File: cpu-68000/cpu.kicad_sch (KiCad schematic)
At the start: 21 parts

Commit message: added memory, peripherals
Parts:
- removed C?: 100nF, symbol Device:C_Small
- removed X?: 10MHz, Oscillator:Oscillator_DIP-8, symbol Oscillator:CXO_DIP8
- added C?: 22µF, symbol Device:C_Polarized_Small
- added C?: 100nF, symbol Device:C_Small
- added C?: 1µF, symbol Device:C_Small
- added R?: 1k, symbol Device:R_Small
- added R? (x2): 10k, symbol Device:R_Small
- added U? (x2): 74HC05, symbol 74xx:74LS05
- added U?: TL7733B, symbol Power_Supervisor:TL7733B
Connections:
- net +5V: now also C?.1, R?.2, U?.7 (SENSE), U?.8 (VCC)
- net GND: now also C?.2, C?.2, C?.2, R?.1, U?.4 (GND)
- net ~{HALT}: now also U?.8
- net ~{RESET}: now also U?.6
- new net: C?.1, U?.1 (REF)
- new net: C?.1, R?.1
- new net: R?.2, U?.3 (CT)
- new net: R?.1, U?.5 (~{RESET})
- new net POR: R?.2, U?.5, U?.6 (RESET), U?.9
- new net ~{MRES}: U?.2 (~{RESIN})
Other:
- note added: "Power on Reset Circuit"

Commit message: Peripherals and general connection stuff
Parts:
- removed C?: 100nF, symbol Device:C_Small
- removed D?: LED_Dual_AKAK, symbol Device:LED_Dual_AKAK
- removed R? (x2): 1k, symbol Device:R_Small
- removed U? (x4): 74HC04, symbol 74xx:74HC04
- added RN? (x2): 10k, Resistor_THT:R_Array_SIP9, symbol Device:R_Network08
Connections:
- net AS: now also U?.15 (IO2)
- net D0: now also RN?.9 (R8)
- net D1: now also RN?.8 (R7)
- net D10: now also RN?.7 (R6)
- net D11: now also RN?.6 (R5)
- net D12: now also RN?.5 (R4)
- net D13: now also RN?.4 (R3)
- net D14: now also RN?.3 (R2)
- net D15: now also RN?.2 (R1)
- net D2: now also RN?.7 (R6)
- net D3: now also RN?.6 (R5)
- net D4: now also RN?.5 (R4)
- net D5: now also RN?.4 (R3)
- net D6: now also RN?.3 (R2)
- net D7: now also RN?.2 (R1)
- net D8: now also RN?.9 (R8)
- net D9: now also RN?.8 (R7)
- net GND: now also RN?.1 (common), RN?.1 (common)
- net ~{AS}: now also U?.14 (IO1)
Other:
- note added: "IRQ Level Encoder"
- note added: "IRQ, addr space decoder"

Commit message: More backplane stuff; added footprints for most
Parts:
- removed C?: 22µF, symbol Device:C_Polarized_Small
- added R301: 1k, Resistor_SMD:R_0805_2012Metric, symbol Device:R_Small
- added R302, R303: 10k, Resistor_SMD:R_0805_2012Metric, symbol Device:R_Small
- C301: renamed from C?; footprint (none) -> Capacitor_Tantalum_SMD:CP_EIA-3216-18_Kemet-A
- C302, C303, C304, C306, C307, C308, C309, C310: renamed from C?; footprint (none) -> Capacitor_SMD:C_0805_2012Metric
- R304, R305, R306: renamed from R?; footprint (none) -> Resistor_SMD:R_0805_2012Metric
- U104: renamed from U?; footprint (none) -> Package_SO:SOIC-14_3.9x8.7mm_P1.27mm
- U301: renamed from U?; footprint Package_LCC:PLCC-68 -> Package_LCC:PLCC-68_THT-Socket
- U303: renamed from U?; footprint (none) -> Package_SO:SOIC-8_3.9x4.9mm_P1.27mm
- U304: renamed from U?; footprint (none) -> Package_SO:TSSOP-16_4.4x5mm_P0.65mm; MPN (none) -> 74HC175PW,118
- gave numbers to parts that had none: 4
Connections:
- net +5V: now also R301.1, R302.1, R303.1
- net ~{BGACK}: now also R303.2
- net ~{BR}: now also R302.2
- net ~{DTACK}: now also R301.2

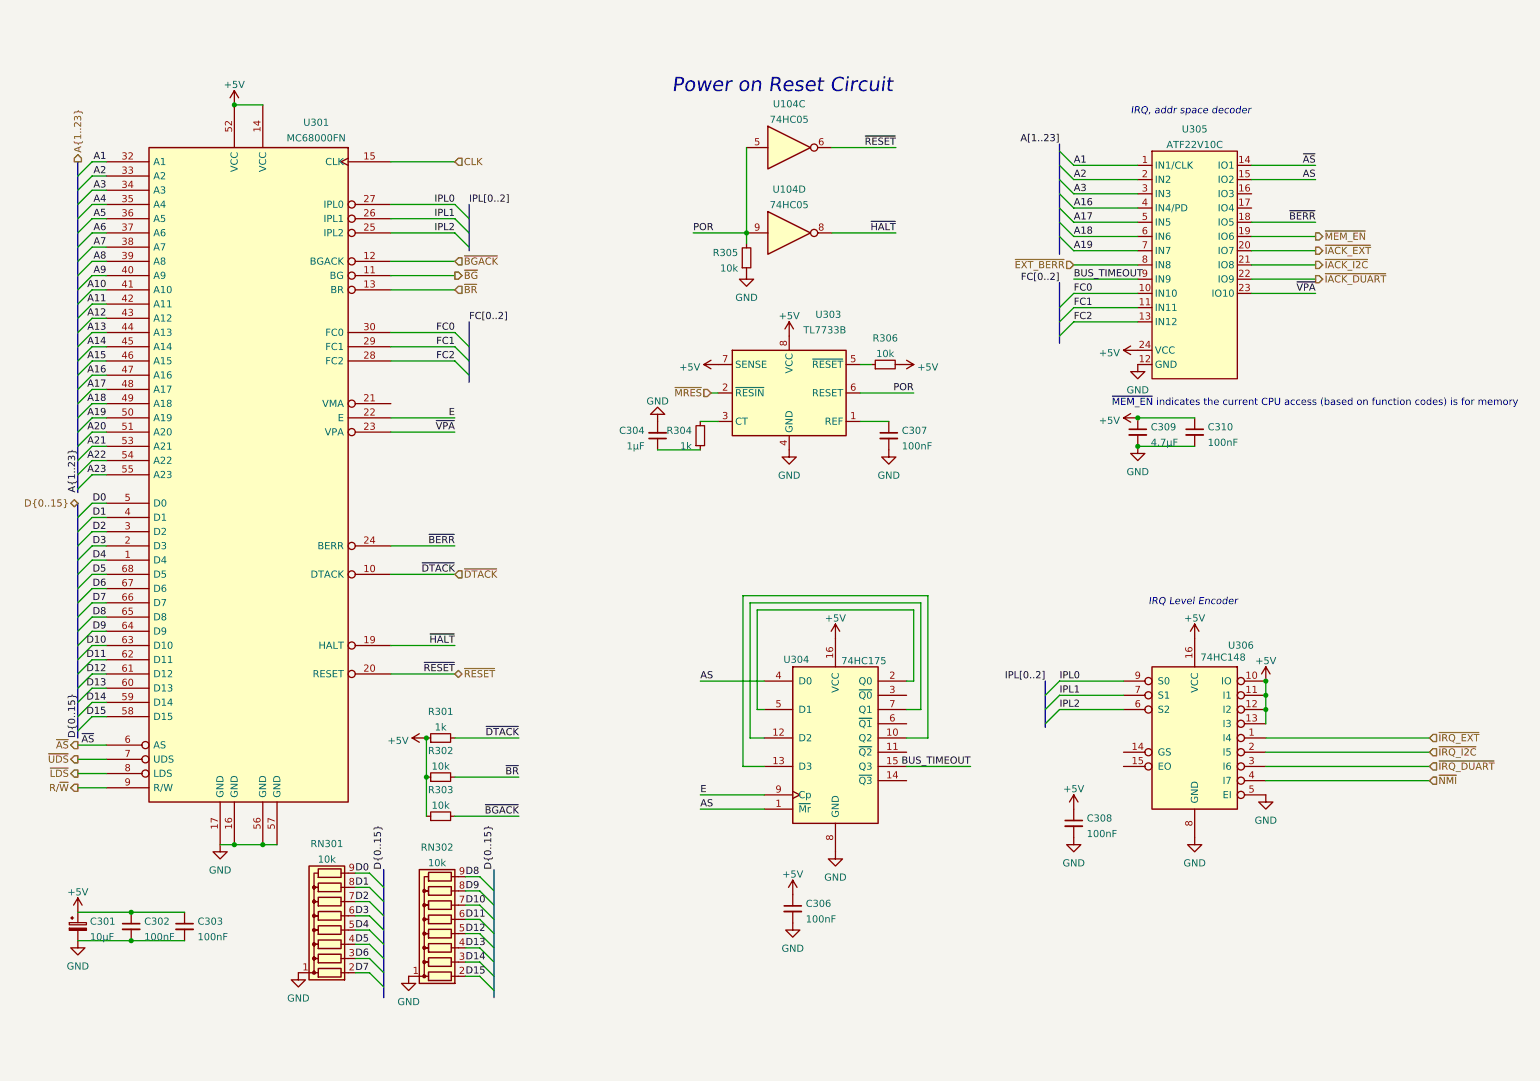
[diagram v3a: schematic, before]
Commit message: start pcb for main cpu
- mostly finish schematic for 68000 cpu; added the missing reset/NMI
  switches

- added footprints for LED indicators

- also added 3d models for fuses, DIN connector, etc
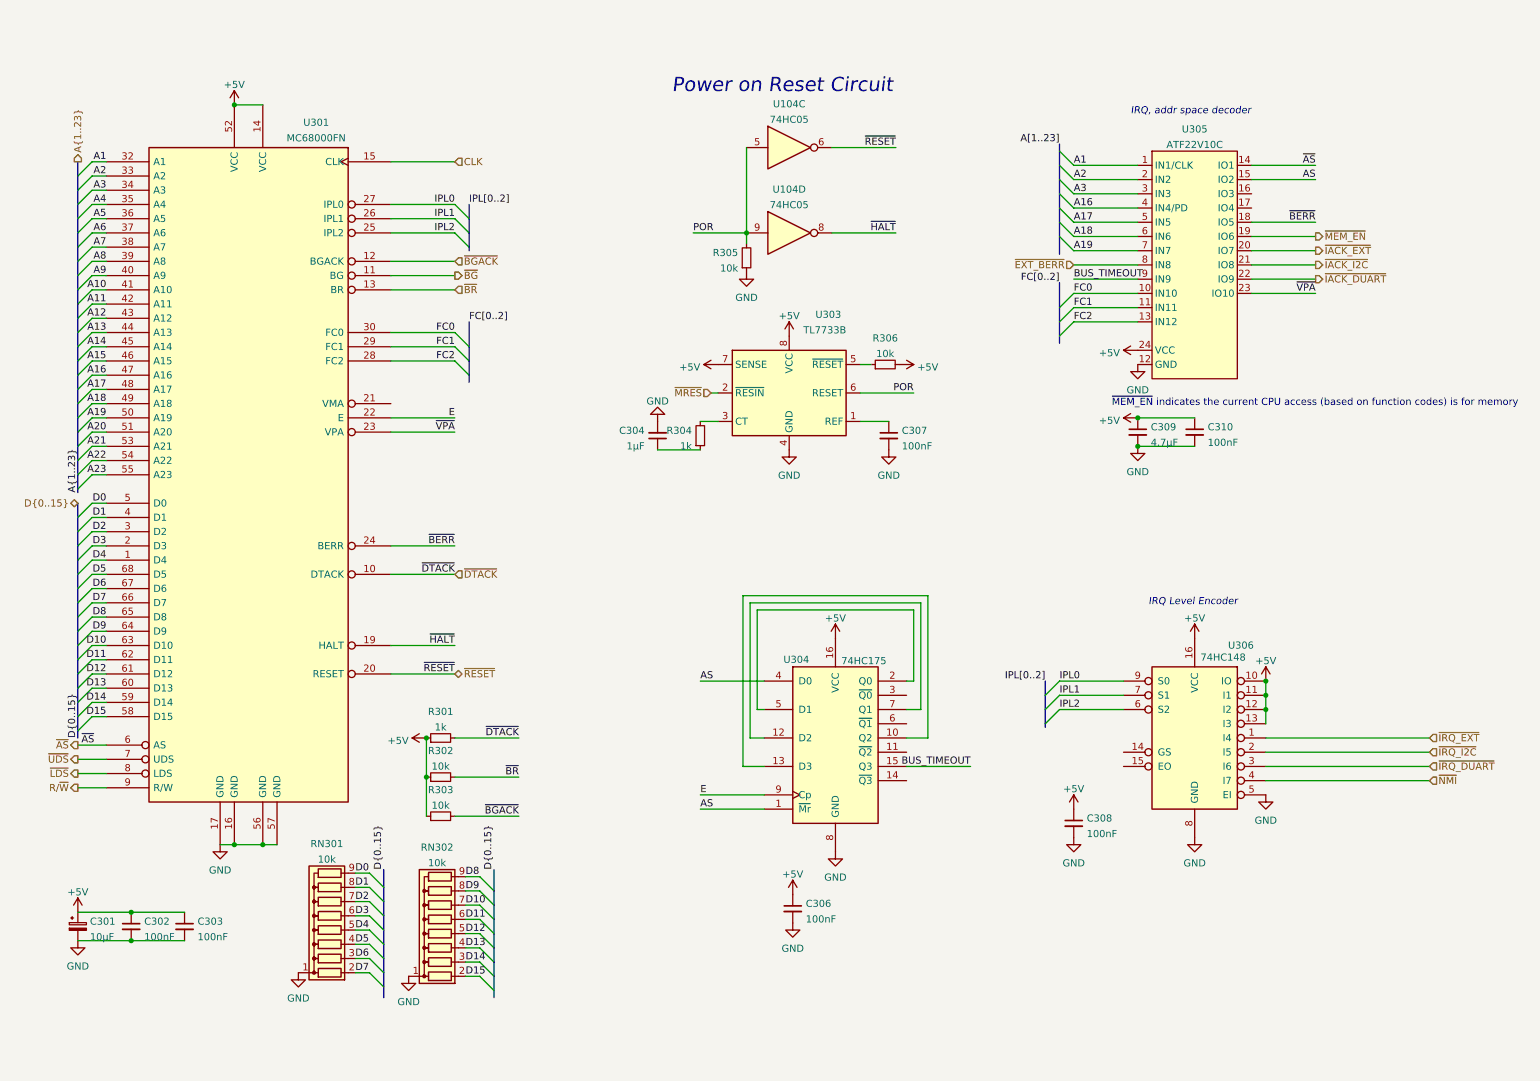
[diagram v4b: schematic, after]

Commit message: Placed most items on pcb
- Laid out most components where they should go on the board; mostly
  routed the connector side of the bus buffers and the address bus

- Added 3d models for PLCC sockets, RTC clock module
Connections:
- net A1: now also U305.2 (IN2); no longer U305.1 (IN1/CLK)
- net A16: now also U305.5 (IN5); no longer U305.4 (IN4/PD)
- net A17: now also U305.6 (IN6); no longer U305.5 (IN5)
- net A18: now also U305.7 (IN7); no longer U305.6 (IN6)
- net A19: now also U305.8 (IN8); no longer U305.7 (IN7)
- net A2: now also U305.3 (IN3); no longer U305.2 (IN2)
- net A3: now also U305.4 (IN4/PD); no longer U305.3 (IN3)
- net BUS_TIMEOUT: now also U305.11 (IN11); no longer U305.9 (IN9)
- net FC0: now also U305.9 (IN9); no longer U305.10 (IN10)
- net FC1: now also U305.10 (IN10); no longer U305.11 (IN11)
- net ~{BERR}: now also U305.22 (IO9); no longer U305.18 (IO5)
- net ~{EXT_BERR}: now also U305.1 (IN1/CLK); no longer U305.8 (IN8)
- net ~{IACK_DUART}: now also U305.17 (IO4); no longer U305.22 (IO9)
- net ~{IACK_EXT}: now also U305.23 (IO10); no longer U305.20 (IO7)
- net ~{IACK_I2C}: now also U305.18 (IO5); no longer U305.21 (IO8)
- net ~{MEM_EN}: now also U305.16 (IO3); no longer U305.19 (IO6)
- net ~{VPA}: now also U305.21 (IO8); no longer U305.23 (IO10)
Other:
- note added: "TODO: Add pulldowns to FC"

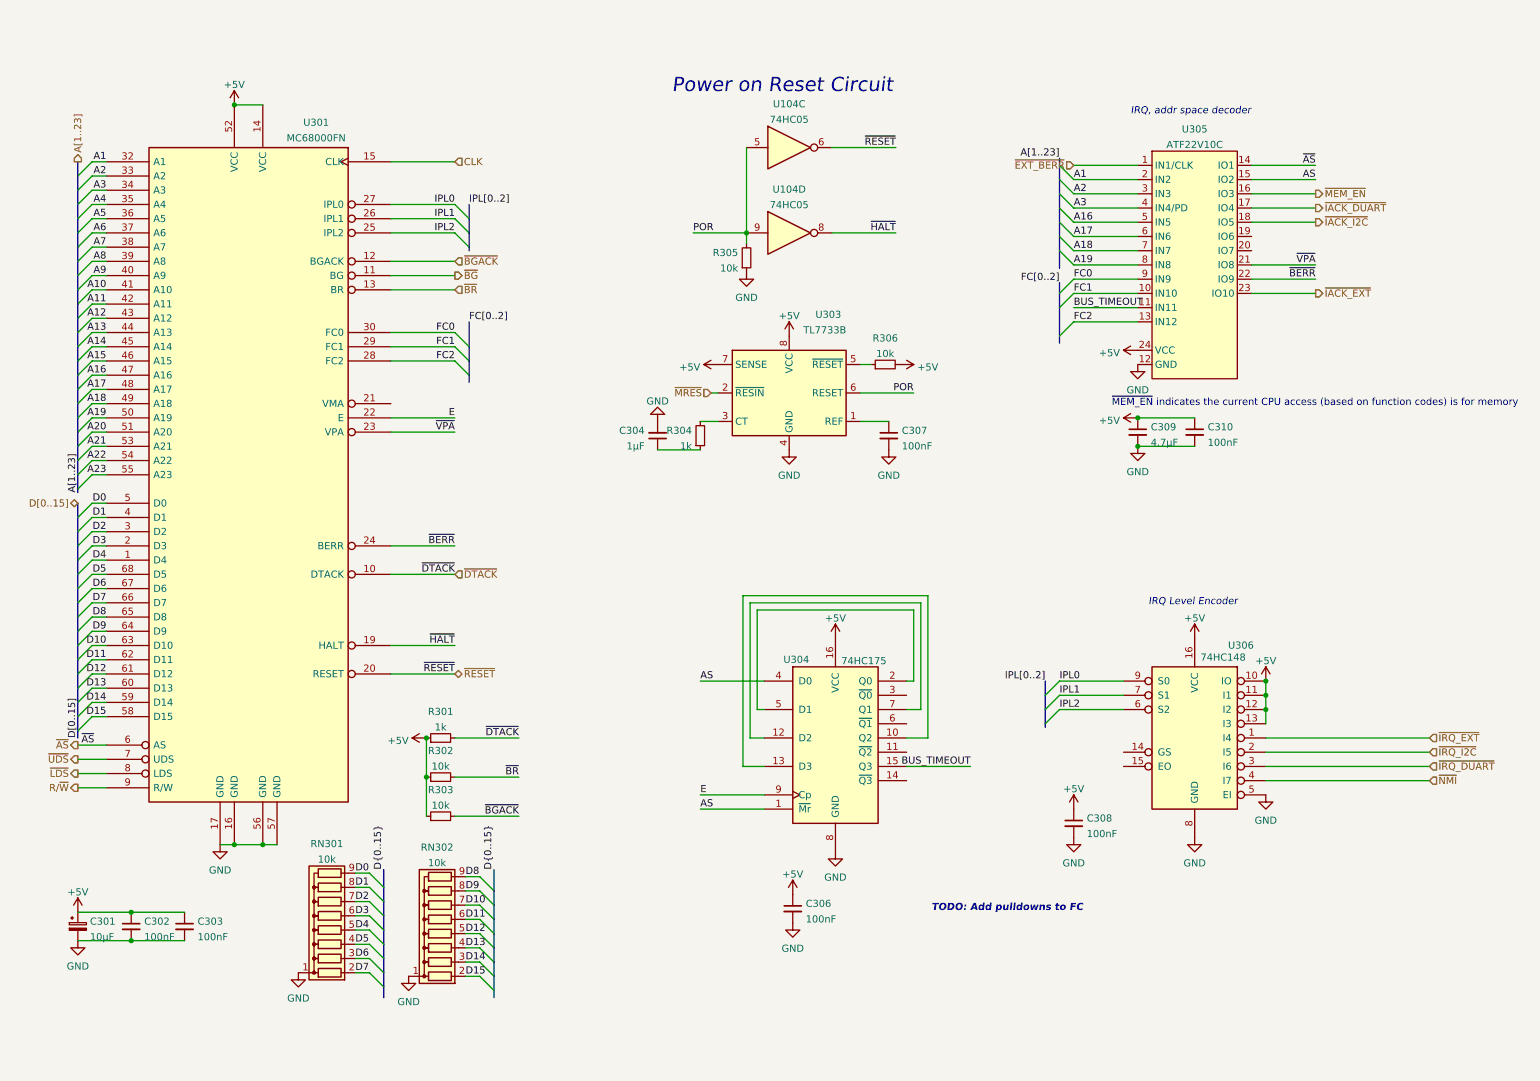
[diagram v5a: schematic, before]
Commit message: Begin routing stuff
- Routed most control signals to GALs, finished routing signals to bus
  transceivers (except data bus)

- Removed ROMs but doubled up RAM; the boot ROM will be provided by an
  external board

- Added dual SAA1099 chips (audio out via backplane)

- Pullups on some external irq/bus request lines
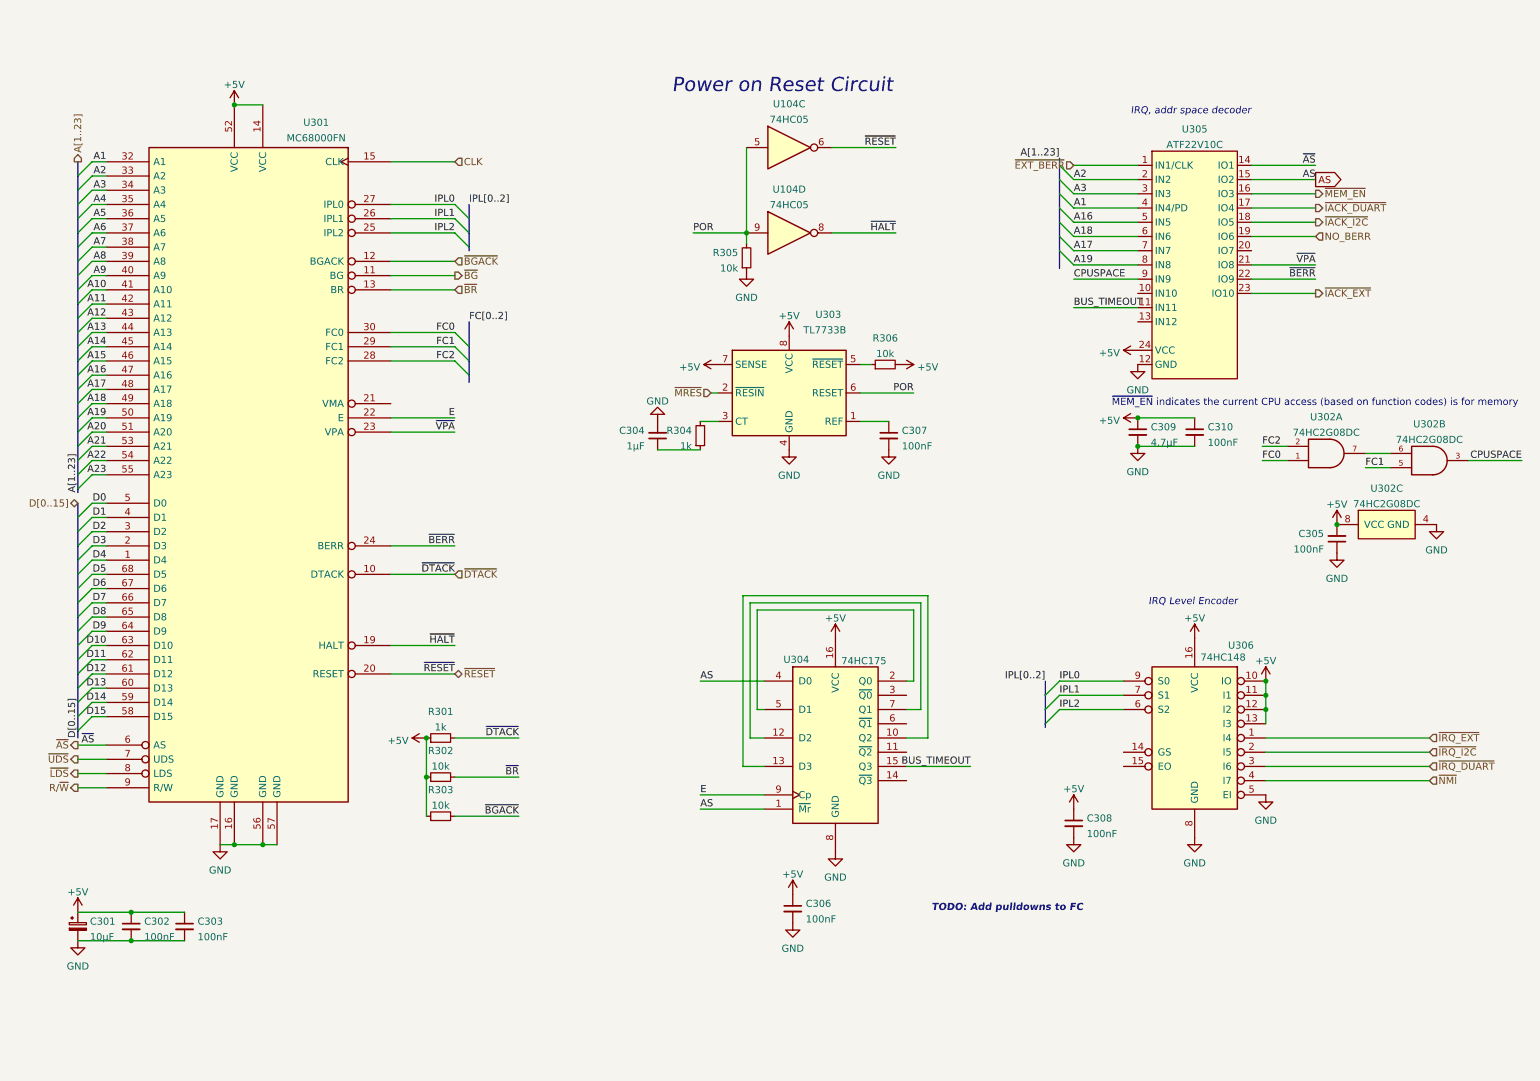
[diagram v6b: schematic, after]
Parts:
- removed RN301, RN302: 10k, Resistor_THT:R_Array_SIP9, symbol Device:R_Network08
- added C305: 100nF, Capacitor_SMD:C_0805_2012Metric, symbol Device:C_Small
- added U302: 74HC2G08DC, Package_SO:VSSOP-8_2.3x2mm_P0.5mm, symbol 68komputer-common:74HC2G08DC
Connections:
- net +5V: now also C305.2, U302.8 (VCC)
- net A1: now also U305.4 (IN4/PD); no longer U305.2 (IN2)
- net A17: now also U305.7 (IN7); no longer U305.6 (IN6)
- net A18: now also U305.6 (IN6); no longer U305.7 (IN7)
- net A2: now also U305.2 (IN2); no longer U305.3 (IN3)
- net A3: now also U305.3 (IN3); no longer U305.4 (IN4/PD)
- net FC0: now also U302.1; no longer U305.9 (IN9)
- net FC1: now also U302.5; no longer U305.10 (IN10)
- net FC2: now also U302.2; no longer U305.13 (IN12)
- net GND: now also C305.1, U302.4 (GND)
- net NO_BERR: now reaches U305.19 (IO6)
- new net: U302.6, U302.7
- new net CPUSPACE: U302.3, U305.9 (IN9)
